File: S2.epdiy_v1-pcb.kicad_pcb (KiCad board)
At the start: 4 copper layers, 106.6 x 58.9 mm, 84 parts, among them J1 USB_C_Receptacle_USB2.0, J2 Jack-DC, P1 CONN_02X13, SW1 RESET, SW2 BOOT, U1 MCP1700-1202E_SOT23, U11 TP4056, U2 ESP32-S2-WROVER, U3 QFN50P700X700X100-49N, U6 ED060XC5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

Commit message: Passes DRC
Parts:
- added TP33: TestPoint, TestPoint:TestPoint_Pad_2.0x2.0mm, F.Cu at (173.8, 116.6)
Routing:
- net EPD_VDD: track 70.1 -> 73.4 mm
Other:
- board text added: "Eink 3.3V >"
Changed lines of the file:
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@@
     )
   )
+  (footprint "TestPoint:TestPoint_Pad_2.0x2.0mm" (layer "F.Cu")
+    (at 173.83 116.61)
+    (descr "SMD rectangular pad as test Point, square 2.0mm side length")
+    (tags "test point SMD pad rectangle square")
+    (property "Sheetfile" "S2.epdiy_v1-pcb.kicad_sch")
+    (property "Sheetname" "")
+    (attr exclude_from_pos_files)
+    (fp_text reference "TP33" (at 0.04 1.81) (layer "F.SilkS")
+      (effects (font (size 0.6 0.6) (thickness 0.1)))
+    )
+    (fp_text value "TestPoint" (at 0 2.05) (layer "F.Fab")
+      (effects (font (size 1 1) (thickness 0.15)))
+    )
+    (fp_text user "${REFERENCE}" (at 0 -2) (layer "F.Fab")
+      (effects (font (size 1 1) (thickness 0.15)))
+    )
+    (fp_line (start 1.2 -1.2) (end 1.2 1.2) (layer "F.SilkS") (width 0.12))
+    (fp_line (start 1.2 1.2) (end -1.2 1.2) (layer "F.SilkS") (width 0.12))
+    (fp_line (start -1.2 -1.2) (end 1.2 -1.2) (layer "F.SilkS") (width 0.12))
+    (fp_line (start -1.2 1.2) (end -1.2 -1.2) (layer "F.SilkS") (width 0.12))
+    (fp_line (start 1.5 1.5) (end 1.5 -1.5) (layer "F.CrtYd") (width 0.05))
+    (fp_line (start 1.5 1.5) (end -1.5 1.5) (layer "F.CrtYd") (width 0.05))
+    (fp_line (start -1.5 -1.5) (end 1.5 -1.5) (layer "F.CrtYd") (width 0.05))
+    (fp_line (start -1.5 -1.5) (end -1.5 1.5) (layer "F.CrtYd") (width 0.05))
+    (pad "1" smd rect (at 0 0) (size 2 2) (layers "F.Cu" "F.Mask")
+      (net 6 "EPD_VDD") (pinfunction "1") (pintype "passive"))
+  )
   (footprint "Capacitor_SMD:C_0805_2012Metric" (layer "F.Cu")
     (at 132.16 97.592 90)
@@
     (effects (font (size 1 1) (thickness 0.1)))
   )
+  (gr_text "Eink 3.3V >" (at 168.81 116.68) (layer "F.SilkS")
+    (effects (font (size 0.8 0.8) (thickness 0.1)))
+  )
   (gr_text "x" (at 113.987664 74.516666 90) (layer "F.SilkS")
     (effects (font (size 1 1) (thickness 0.15)))
@@
   (segment (start 132.1825 108.735) (end 132.1825 109.762276) (width 0.25) (layer "F.Cu") (net 6))
   (segment (start 134.687935 111.170065) (end 136.612 113.09413) (width 0.3) (layer "F.Cu") (net 6))
+  (segment (start 172.325 116.61) (end 171.02 115.305) (width 0.25) (layer "F.Cu") (net 6))
   (segment (start 132.774713 110.354489) (end 133.892459 110.354489) (width 0.25) (layer "F.Cu") (net 6))
   (segment (start 136.612 113.09413) (end 136.612 115.246) (width 0.3) (layer "F.Cu") (net 6))
@@
   (segment (start 143.82512 115.51712) (end 144.304 115.996) (width 0.3) (layer "F.Cu") (net 6))
   (segment (start 144.304 115.996) (end 170.329 115.996) (width 0.3) (layer "F.Cu") (net 6))
+  (segment (start 173.83 116.61) (end 172.325 116.61) (width 0.25) (layer "F.Cu") (net 6))
   (segment (start 136.88312 115.51712) (end 143.82512 115.51712) (width 0.3) (layer "F.Cu") (net 6))
   (segment (start 185.295 107.705) (end 185.245 107.755) (width 0.25) (layer "F.Cu") (net 6))

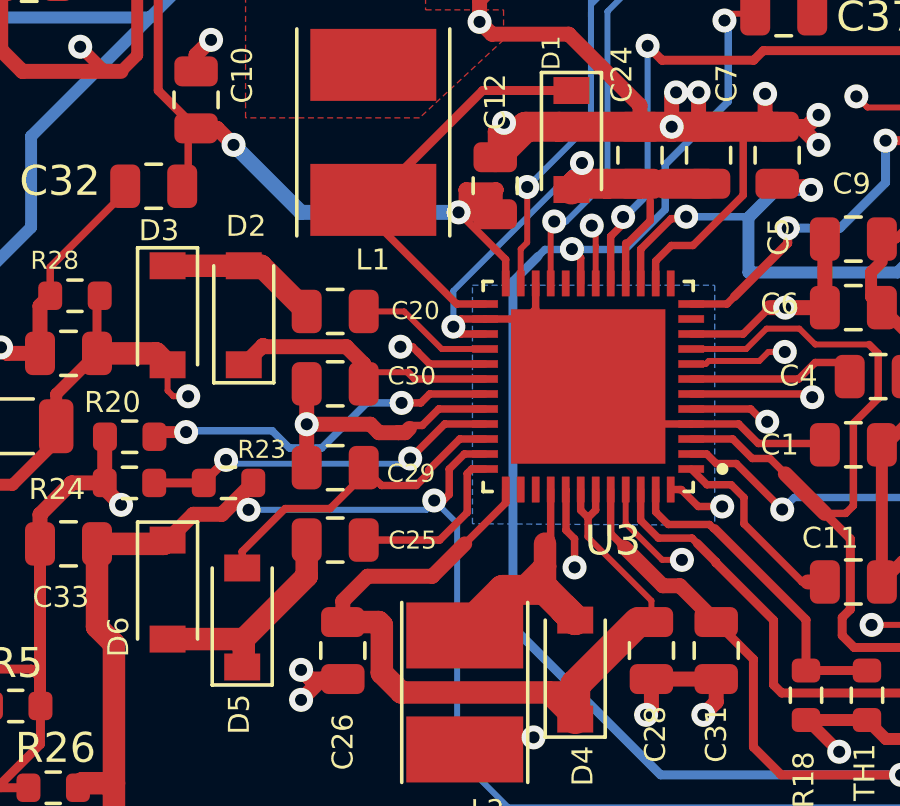
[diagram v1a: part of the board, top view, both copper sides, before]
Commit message: 16 VNEG_IN was not connected properly
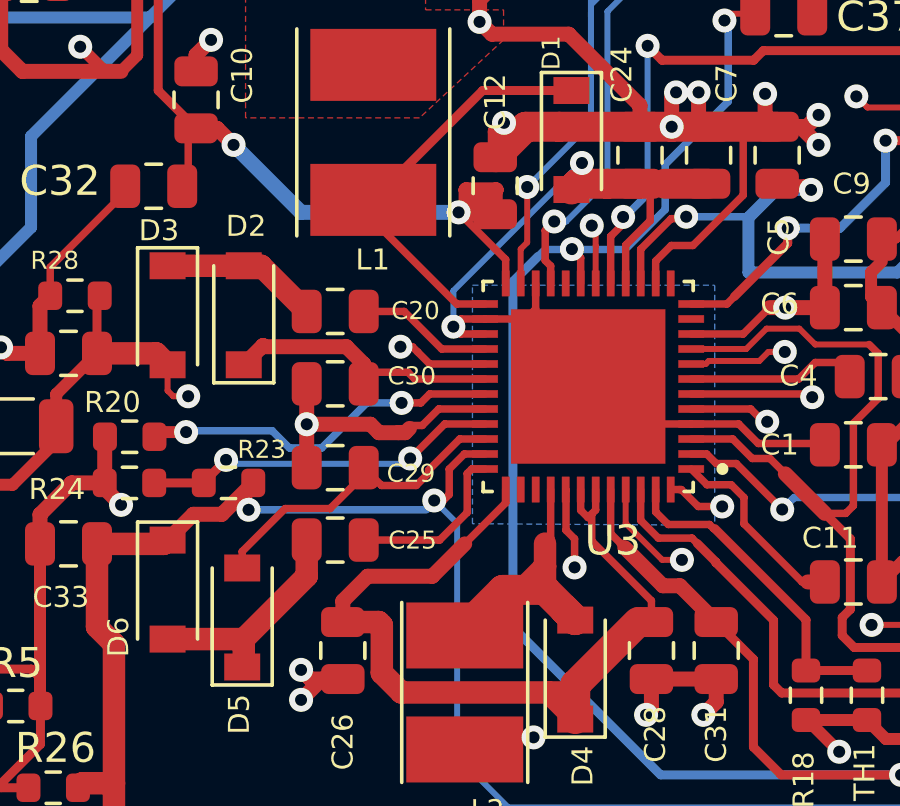
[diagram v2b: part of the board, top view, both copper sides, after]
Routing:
- net /+22V: track 153.3 -> 154.2 mm
- net /VNEG_IN: track 27.8 -> 28.6 mm
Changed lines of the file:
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@@
   (segment (start 118.5745 109.2085) (end 118.910502 109.2085) (width 0.3) (layer "F.Cu") (net 29))
   (segment (start 116.412 110.42) (end 117.272001 109.559999) (width 0.5) (layer "F.Cu") (net 29))
+  (segment (start 119.112 108.671) (end 119.269 108.514) (width 0.25) (layer "F.Cu") (net 29))
+  (segment (start 119.112 109.409998) (end 119.112 108.671) (width 0.25) (layer "F.Cu") (net 29))
   (segment (start 118.5745 109.2085) (end 119.269 108.514) (width 0.5) (layer "F.Cu") (net 29))
   (segment (start 114.06 110.546) (end 116.286 110.546) (width 0.75) (layer "F.Cu") (net 29))
@@
   (via (at 185.12 85.08) (size 0.8) (drill 0.4) (layers "F.Cu" "B.Cu") (net 29))
   (via (at 125.3 109.1) (size 0.8) (drill 0.4) (layers "F.Cu" "B.Cu") (net 29))
+  (segment (start 125.041002 109.409998) (end 125.041002 109.358998) (width 0.2) (layer "B.Cu") (net 29))
   (segment (start 127.77 119.33) (end 187.22 119.33) (width 0.2) (layer "B.Cu") (net 29))
   (segment (start 126.064 109.864) (end 126.064 109.936) (width 0.2) (layer "B.Cu") (net 29))
-  (segment (start 125.041002 109.409998) (end 119.112 109.409998) (width 0.2) (layer "B.Cu") (net 29))
+  (segment (start 125.041002 109.409998) (end 119.112 109.409998) (width 0.25) (layer "B.Cu") (net 29))
   (segment (start 193.745 93.705) (end 185.12 85.08) (width 0.2) (layer "B.Cu") (net 29))
   (segment (start 125.041002 109.358998) (end 125.3 109.1) (width 0.2) (layer "B.Cu") (net 29))
   (segment (start 187.22 119.33) (end 193.745 112.805) (width 0.2) (layer "B.Cu") (net 29))
   (segment (start 126.064 109.936) (end 126.064 117.624) (width 0.2) (layer "B.Cu") (net 29))
-  (segment (start 125.041002 109.409998) (end 125.041002 109.358998) (width 0.2) (layer "B.Cu") (net 29))
   (segment (start 193.745 112.805) (end 193.745 93.705) (width 0.2) (layer "B.Cu") (net 29))
   (segment (start 125.3 109.1) (end 126.064 109.864) (width 0.2) (layer "B.Cu") (net 29))
@@
   (segment (start 159.425 102.35) (end 159.42 102.355) (width 0.2) (layer "F.Cu") (net 40))
   (segment (start 129.4 99.8) (end 129.3 99.8) (width 0.2) (layer "F.Cu") (net 40))
+  (segment (start 129.1825 101.865) (end 129.1825 101.2825) (width 0.25) (layer "F.Cu") (net 40))
   (segment (start 129.1825 100.0175) (end 129.4 99.8) (width 0.2) (layer "F.Cu") (net 40))
-  (segment (start 129.1825 101.865) (end 129.1825 100.0175) (width 0.2) (layer "F.Cu") (net 40))
+  (segment (start 129 100.1) (end 129.3 99.8) (width 0.25) (layer "F.Cu") (net 40))
+  (segment (start 129 101.1) (end 129 100.1) (width 0.25) (layer "F.Cu") (net 40))
   (segment (start 159.425 97.7) (end 159.425 102.35) (width 0.2) (layer "F.Cu") (net 40))
+  (segment (start 129.1825 101.2825) (end 129 101.1) (width 0.25) (layer "F.Cu") (net 40))
   (via (at 129.3 99.8) (size 0.8) (drill 0.4) (layers "F.Cu" "B.Cu") (net 40))
   (via (at 159.425 97.7) (size 0.8) (drill 0.4) (layers "F.Cu" "B.Cu") (net 40))
@@
   (segment (start 92.125 102.075) (end 93.225 100.975) (width 0.4) (layer "F.Cu") (net 42))
   (segment (start 131.067 98.542) (end 130.066 98.542) (width 1) (layer "F.Cu") (net 43))
+  (segment (start 132.5 99.769649) (end 132.5 98.882) (width 0.25) (layer "F.Cu") (net 43))
   (segment (start 135.45 106.55) (end 136.1 107.2) (width 0.25) (layer "F.Cu") (net 43))
   (segment (start 126.9975 103.05) (end 126.194 103.05) (width 0.25) (layer "F.Cu") (net 43))
@@
   (segment (start 128.35 103.05) (end 128.6825 102.7175) (width 0.25) (layer "F.Cu") (net 43))
   (segment (start 138.278 107.2) (end 138.322 107.244) (width 0.25) (layer "F.Cu") (net 43))
-  (segment (start 132.5 99.769649) (end 132.5 99.1) (width 0.25) (layer "F.Cu") (net 43))
   (segment (start 130.066 98.542) (end 129.874 98.734) (width 1) (layer "F.Cu") (net 43))
+  (segment (start 132.5 98.882) (end 132.16 98.542) (width 0.25) (layer "F.Cu") (net 43))
+  (segment (start 131.6825 100.587149) (end 132.5 99.769649) (width 0.25) (layer "F.Cu") (net 43))
   (segment (start 126.9975 103.55) (end 126.182514 103.55) (width 0.25) (layer "F.Cu") (net 43))
   (segment (start 128.6825 102.7175) (end 128.6825 101.865) (width 0.25) (layer "F.Cu") (net 43))
-  (segment (start 131.6825 101.865) (end 131.6825 100.5175) (width 0.25) (layer "F.Cu") (net 43))
   (segment (start 126.194 103.05) (end 125.938257 103.305743) (width 0.25) (layer "F.Cu") (net 43))
   (segment (start 126.182514 103.55) (end 125.938257 103.305743) (width 0.25) (layer "F.Cu") (net 43))
-  (segment (start 131.752149 100.5175) (end 132.5 99.769649) (width 0.25) (layer "F.Cu") (net 43))
   (segment (start 126.9975 103.05) (end 128.35 103.05) (width 0.25) (layer "F.Cu") (net 43))
   (segment (start 136.1 107.2) (end 138.278 107.2) (width 0.25) (layer "F.Cu") (net 43))
+  (segment (start 131.6825 101.865) (end 131.6825 100.587149) (width 0.25) (layer "F.Cu") (net 43))
   (segment (start 131.6825 106.55) (end 130.4325 105.3) (width 0.25) (layer "F.Cu") (net 43))
   (segment (start 132.983 98.542) (end 134.446 98.542) (width 1) (layer "F.Cu") (net 43))
@@
   (segment (start 119.527 101.276) (end 121.05 102.799) (width 0.75) (layer "F.Cu") (net 59))
   (segment (start 118.952 101.276) (end 119.527 101.276) (width 0.75) (layer "F.Cu") (net 59))
-  (segment (start 124.299 102.799) (end 125.55 104.05) (width 0.2) (layer "F.Cu") (net 60))
-  (segment (start 125.55 104.05) (end 126.9975 104.05) (width 0.2) (layer "F.Cu") (net 60))
-  (segment (start 122.95 102.799) (end 124.299 102.799) (width 0.2) (layer "F.Cu") (net 60))
+  (segment (start 124.299 102.799) (end 125.55 104.05) (width 0.25) (layer "F.Cu") (net 60))
+  (segment (start 125.55 104.05) (end 126.9975 104.05) (width 0.25) (layer "F.Cu") (net 60))
+  (segment (start 122.95 102.799) (end 124.299 102.799) (width 0.25) (layer "F.Cu") (net 60))
   (segment (start 118.952 113.72) (end 118.952 114.598) (width 0.75) (layer "F.Cu") (net 61))
   (segment (start 121.05 111.622) (end 118.952 113.72) (width 0.75) (layer "F.Cu") (net 61))
@@
   (segment (start 122.254 112.451) (end 123.0795 111.6255) (width 0.5) (layer "F.Cu") (net 63))
   (segment (start 123.55352 114.847522) (end 123.55352 113.25352) (width 0.75) (layer "F.Cu") (net 63))
-  (segment (start 132.541 112.441) (end 130.4 110.3) (width 0.2) (layer "F.Cu") (net 63))
   (segment (start 123.0795 111.6255) (end 125.2385 111.6255) (width 0.5) (layer "F.Cu") (net 63))
   (segment (start 124.204998 115.499) (end 123.55352 114.847522) (width 0.75) (layer "F.Cu") (net 63))
-  (segment (start 132.541 113.152) (end 132.541 112.441) (width 0.2) (layer "F.Cu") (net 63))
+  (segment (start 132.541 113.152) (end 132.541 112.441) (width 0.25) (layer "F.Cu") (net 63))
   (segment (start 130.6825 108.735) (end 130.6825 109.4175) (width 0.25) (layer "F.Cu") (net 63))
   (segment (start 127.6825 108.735) (end 127.6825 109.1815) (width 0.25) (layer "F.Cu") (net 63))
   (segment (start 130.001 115.245) (end 132.094 113.152) (width 1) (layer "F.Cu") (net 63))
+  (segment (start 132.541 112.441) (end 130.55 110.45) (width 0.25) (layer "F.Cu") (net 63))
   (segment (start 129.747 115.499) (end 130.001 115.245) (width 0.75) (layer "F.Cu") (net 63))
-  (segment (start 130.428801 109.671199) (end 130.428801 110.3) (width 0.25) (layer "F.Cu") (net 63))
   (segment (start 129.113 115.499) (end 130.001 116.387) (width 0.75) (layer "F.Cu") (net 63))
   (segment (start 130.1825 108.735) (end 130.1825 109.424898) (width 0.25) (layer "F.Cu") (net 63))
   (segment (start 130.001 116.387) (end 130.001 115.245) (width 1) (layer "F.Cu") (net 63))
+  (segment (start 130.6825 109.4175) (end 130.55 109.55) (width 0.25) (layer "F.Cu") (net 63))
+  (segment (start 130.55 110.45) (end 130.55 109.55) (width 0.25) (layer "F.Cu") (net 63))
   (segment (start 122.254 113.152) (end 122.254 112.451) (width 0.5) (layer "F.Cu") (net 63))
-  (segment (start 130.6825 109.4175) (end 130.428801 109.671199) (width 0.25) (layer "F.Cu") (net 63))
+  (segment (start 130.55 109.55) (end 130.428801 109.671199) (width 0.25) (layer "F.Cu") (net 63))
   (segment (start 129.113 115.499) (end 124.204998 115.499) (width 0.75) (layer "F.Cu") (net 63))
   (segment (start 129.113 115.499) (end 129.747 115.499) (width 0.75) (layer "F.Cu") (net 63))
@@
   (segment (start 119.59399 103.93401) (end 119.6335 103.97352) (width 0.5) (layer "F.Cu") (net 65))
   (segment (start 118.952 104.576) (end 119.59399 103.93401) (width 0.5) (layer "F.Cu") (net 65))
-  (segment (start 124.425 104.825) (end 123.337 104.825) (width 0.2) (layer "F.Cu") (net 65))
+  (segment (start 124.425 104.825) (end 123.337 104.825) (width 0.25) (layer "F.Cu") (net 65))
   (segment (start 119.6335 103.97352) (end 122.37352 103.97352) (width 0.5) (layer "F.Cu") (net 65))
   (segment (start 126.916 95.434) (end 123.27 99.08) (width 0.3) (layer "F.Cu") (net 66))

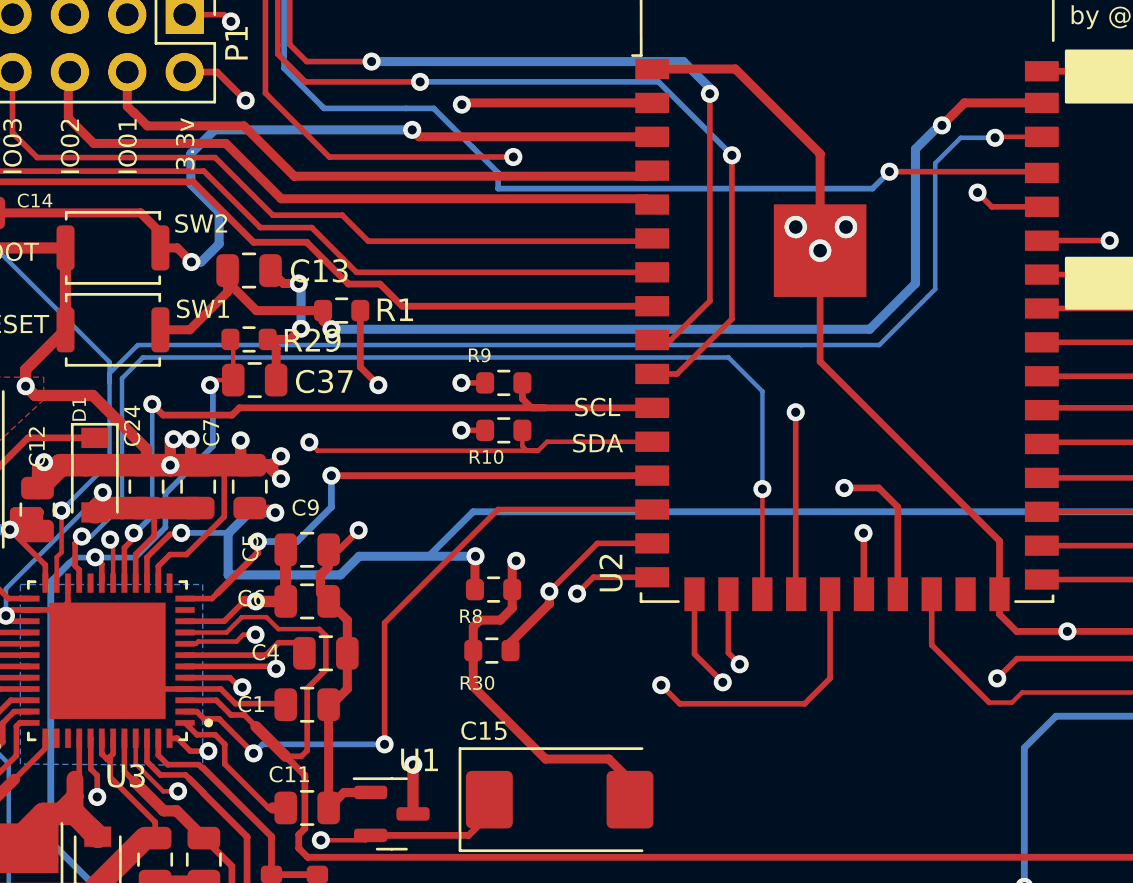
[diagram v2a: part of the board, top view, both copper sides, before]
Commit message: Add TPS_mINT & PWRGOOD pull-ups. Move Wrover board demo
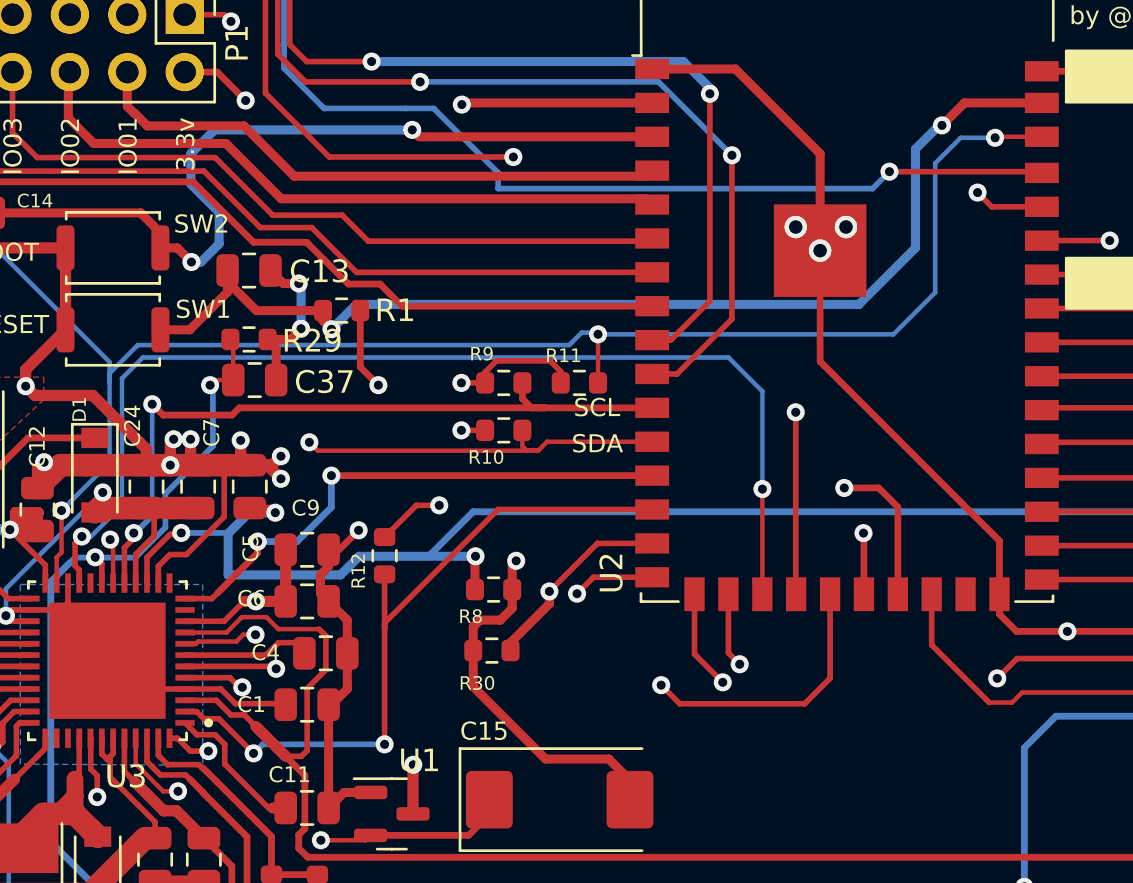
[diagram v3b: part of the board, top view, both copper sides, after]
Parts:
- added R11: 10K, Resistor_SMD:R_0603_1608Metric, F.Cu at (151.3, 93.0)
- added R12: 10K, Resistor_SMD:R_0603_1608Metric, F.Cu at (142.7, 100.7)
- R2, R3: value 1K -> 2K2
- U7: value TPS2113APW -> TPS2113APWR
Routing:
- net /+3.3V: track 89.7 -> 97.4 mm, vias 7 -> 8
- net /TPS_nINT: track 29.1 -> 31.4 mm
- net /TPS_PWR_GOOD: track 95.6 -> 97.9 mm, vias 3 -> 4
- net Net-(C13-Pad1): track 49.9 -> 49.0 mm
